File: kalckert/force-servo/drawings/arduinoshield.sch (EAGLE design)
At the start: 28 parts, among them IC1 MCP604P, IC3 7806T

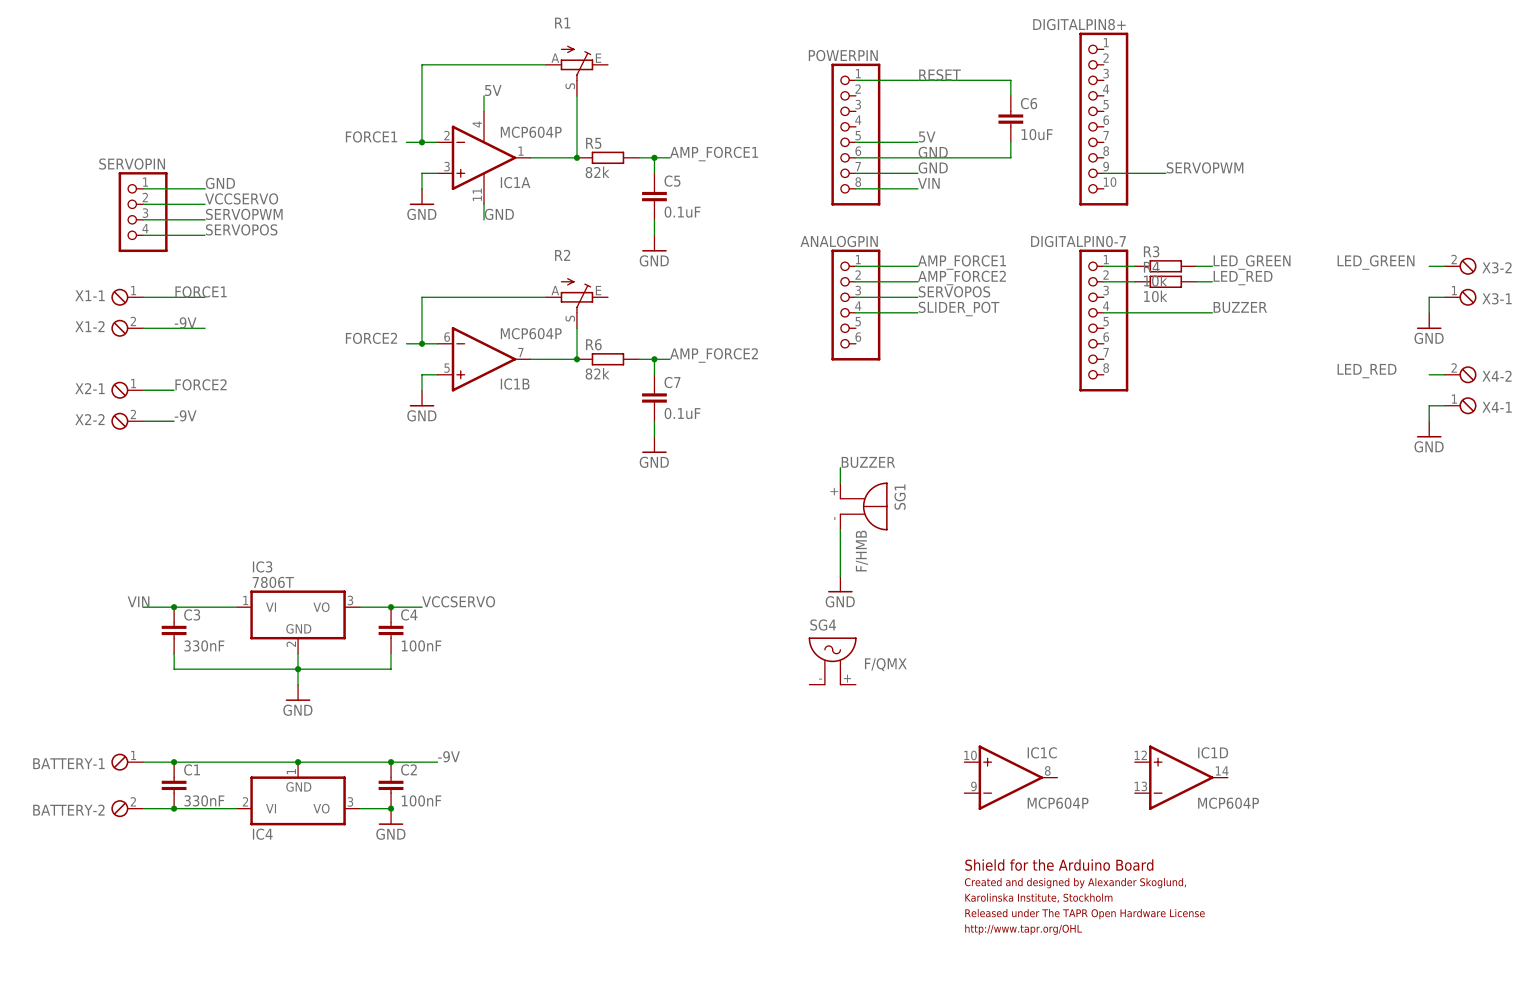
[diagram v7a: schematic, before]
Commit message: Updated power regulator
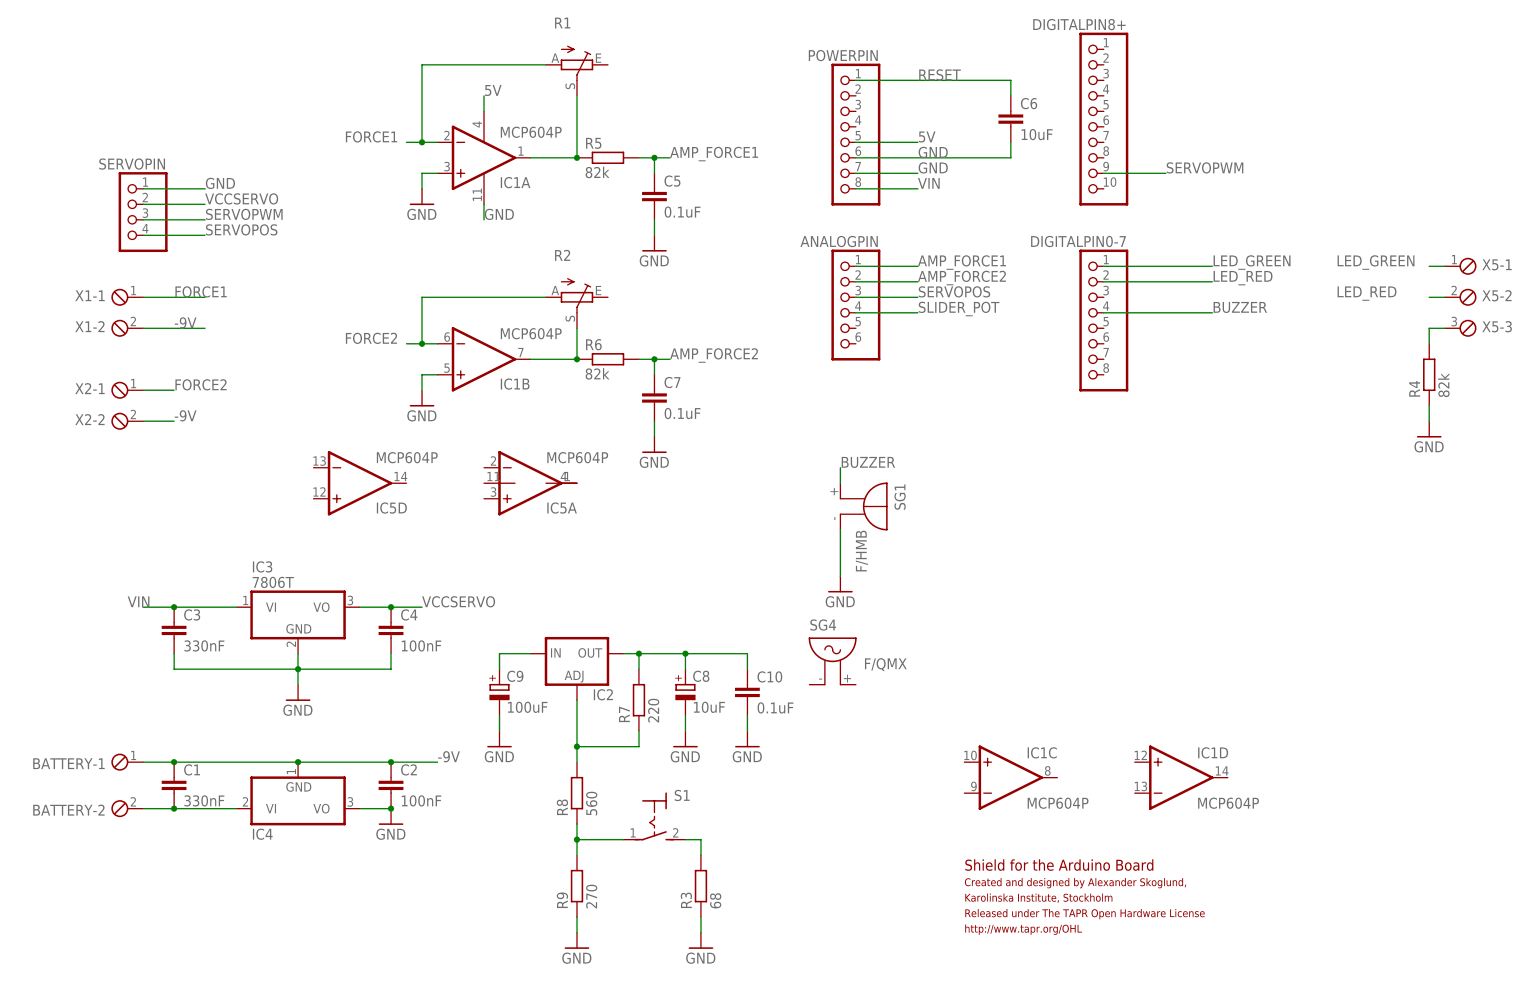
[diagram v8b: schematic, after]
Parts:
- removed X3, X4: (no value), con-phoenix-254:MPT2
- added C10: 0.1uF, resistor:C-EU050-025X075
- added C8: 10uF, resistor:CPOL-EUE2.5-5
- added C9: 100uF, resistor:CPOL-EUE2.5-7
- added IC2: (no value), v-reg:LM317TL
- added IC5: MCP604P, linear:MCP604P
- added R7: 220, resistor:R-EU_0207/7
- added R8: 560, resistor:R-EU_0207/7
- added R9: 270, resistor:R-EU_0207/7
- added S1: (no value), switch:MS243
- added X5: (no value), con-phoenix-254:MPT3
- R3: value 10k -> 68
- R4: value 10k -> 82k
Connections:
- new net N$14: C9.+, IC2.IN
- new net N$19: R8.1, R9.2, S1.P
- new net N$20: C10.1, C8.+, IC2.OUT, R7.2
- new net N$23: IC2.ADJ, R7.1, R8.2
- new net N$5: IC5A.OUT, IC5P.V+
- net GND: now also C10.2, C8.-, C9.-, R3.1, R4.1, R9.1; no longer X3-1.1, X4-1.1
- net LED_GREEN: now also DIGITALPIN0-7.1, X5-1.1; no longer R3.2, X3-2.1
- net LED_RED: now also DIGITALPIN0-7.2, X5-2.1; no longer R4.2, X4-2.1
- net N$1: now also R4.2; no longer DIGITALPIN0-7.1, R3.1
- net N$4: now also R3.2, S1.S; no longer DIGITALPIN0-7.2, R4.1
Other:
- moved on the sheet: R3, R4
